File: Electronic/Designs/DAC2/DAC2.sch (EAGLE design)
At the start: 15 parts

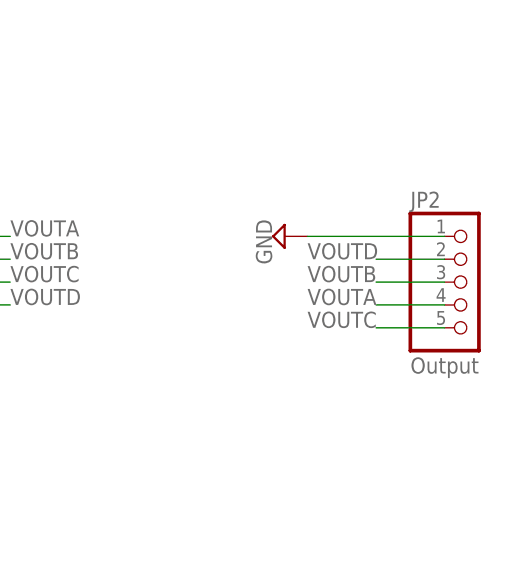
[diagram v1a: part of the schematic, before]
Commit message: Added better Cmake QT Find and added dac2 piezo and tun boards
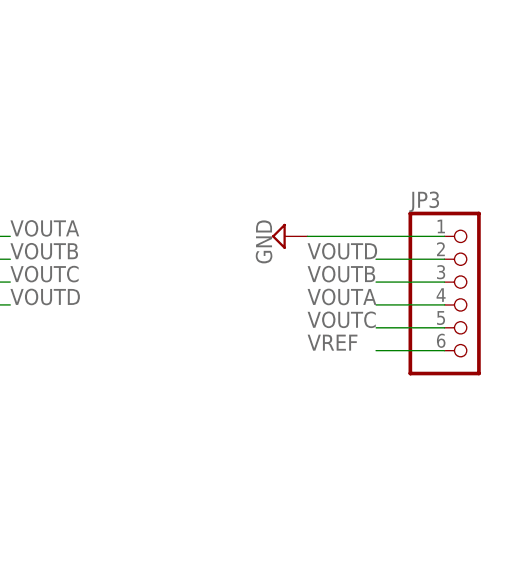
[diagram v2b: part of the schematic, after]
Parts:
- removed JP2: Output, pinhead:PINHD-1X5
- added JP3: (no value), pinhead:PINHD-1X6
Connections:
- net GND: now also JP3.1; no longer JP2.1
- net VOUTA: now also JP3.4; no longer JP2.4
- net VOUTB: now also JP3.3; no longer JP2.3
- net VOUTC: now also JP3.5; no longer JP2.5
- net VOUTD: now also JP3.2; no longer JP2.2
- net VREF: now also JP3.6
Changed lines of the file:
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@@
 <part name="SUPPLY3" library="supply2" deviceset="GND" device=""/>
 <part name="JP1" library="pinhead" deviceset="PINHD-1X9" device="" value="Input"/>
-<part name="JP2" library="pinhead" deviceset="PINHD-1X5" device="" value="Output"/>
 <part name="SUPPLY4" library="supply2" deviceset="GND" device=""/>
 <part name="SUPPLY5" library="supply2" deviceset="GND" device=""/>
+<part name="JP3" library="pinhead" deviceset="PINHD-1X6" device=""/>
 </parts>
 <sheets>
@@
 <instance part="SUPPLY3" gate="GND" x="0" y="-20.32"/>
 <instance part="JP1" gate="A" x="-71.12" y="30.48" rot="R180"/>
-<instance part="JP2" gate="A" x="78.74" y="5.08"/>
 <instance part="SUPPLY4" gate="GND" x="58.42" y="10.16" rot="R270"/>
 <instance part="SUPPLY5" gate="GND" x="-50.8" y="40.64" rot="R90"/>
+<instance part="JP3" gate="A" x="78.74" y="2.54"/>
 </instances>
 <busses>
@@
 </segment>
 <segment>
-<pinref part="JP2" gate="A" pin="4"/>
 <wire x1="76.2" y1="2.54" x2="68.58" y2="2.54" width="0.1524" layer="91"/>
 <label x="60.96" y="2.54" size="1.778" layer="95"/>
+<pinref part="JP3" gate="A" pin="4"/>
 </segment>
 </net>
@@
 </segment>
 <segment>
-<pinref part="JP2" gate="A" pin="3"/>
 <wire x1="76.2" y1="5.08" x2="68.58" y2="5.08" width="0.1524" layer="91"/>
 <label x="60.96" y="5.08" size="1.778" layer="95"/>
+<pinref part="JP3" gate="A" pin="3"/>
 </segment>
 </net>
@@
 </segment>
 <segment>
-<pinref part="JP2" gate="A" pin="5"/>
 <wire x1="76.2" y1="0" x2="68.58" y2="0" width="0.1524" layer="91"/>
 <label x="60.96" y="0" size="1.778" layer="95"/>
+<pinref part="JP3" gate="A" pin="5"/>
 </segment>
 </net>
@@
 </segment>
 <segment>
-<pinref part="JP2" gate="A" pin="2"/>
 <wire x1="76.2" y1="7.62" x2="68.58" y2="7.62" width="0.1524" layer="91"/>
 <label x="60.96" y="7.62" size="1.778" layer="95"/>
+<pinref part="JP3" gate="A" pin="2"/>
 </segment>
 </net>
@@
 <segment>
 <pinref part="SUPPLY4" gate="GND" pin="GND"/>
-<pinref part="JP2" gate="A" pin="1"/>
 <wire x1="60.96" y1="10.16" x2="76.2" y2="10.16" width="0.1524" layer="91"/>
+<pinref part="JP3" gate="A" pin="1"/>
 </segment>
 <segment>
@@
 <label x="43.18" y="101.6" size="1.778" layer="95"/>
 </segment>
-</net>
+<segment>
+<pinref part="JP3" gate="A" pin="6"/>
+<wire x1="76.2" y1="-2.54" x2="68.58" y2="-2.54" width="0.1524" layer="91"/>
+<label x="60.96" y="-2.54" size="1.778" layer="95"/>
+</segment>
+</net>

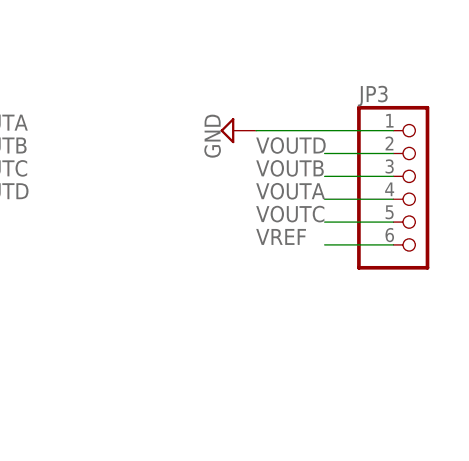
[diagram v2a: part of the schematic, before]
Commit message: added change to DAC2 board
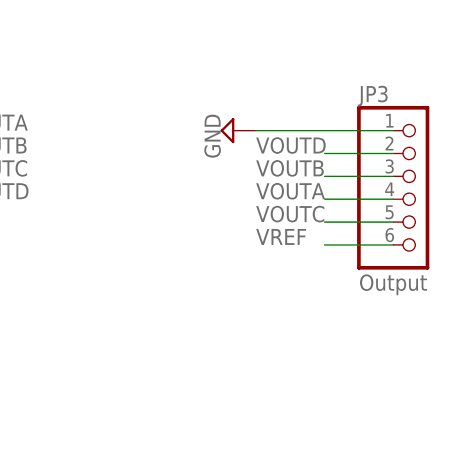
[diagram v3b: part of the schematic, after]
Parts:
- JP3: value (none) -> Output
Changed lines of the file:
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@@
 <part name="SUPPLY4" library="supply2" deviceset="GND" device=""/>
 <part name="SUPPLY5" library="supply2" deviceset="GND" device=""/>
-<part name="JP3" library="pinhead" deviceset="PINHD-1X6" device=""/>
+<part name="JP3" library="pinhead" deviceset="PINHD-1X6" device="" value="Output"/>
 </parts>
 <sheets>
